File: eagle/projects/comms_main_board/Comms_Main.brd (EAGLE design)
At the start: 160 x 100 mm, 187 parts, among them J1 WRL-00593, J10 MOL-SL-2-RA, J11 MOL-SL-3-RA, J12 MOL-SL-3-RA, J13 MOL-SL-3-RA, J14 MOL-SL-3-RA, J15 MOL-SL-2-RA, J16 MOL-MINIJR-2P-RA, J17 MOL-MINIJR-2P-RA, J18 MOL-MINIJR-2P-RA, J19 MOL-MINIJR-2P-RA, J2 PRT-12639, J20 MOL-SL-2-RA, J21 RECEPTACLE-2x2-254MM, J22 MOL-SL-2-RA, J3 PRT-12639, J4 PRT-12639, J5 PRT-12639, J6 MOL-SL-3-RA, J7 MOL-SL-5-RA, J8 RECEPTACLE-2x20-254MM, J9 MOL-SL-3-RA, Q1 CSD17579Q3A, U1 TPS562209DDCT, U10 MCP4541-103E/MS, U11 TPS562209DDCT, U12 MMBT3904-7-F, U13 MAX3232CSE+, U14 MAX4311, U15 MAX6371, U2 LP2985-33DBVR, U3 LP5900TLX-3.3/NOPB, U4 TPS562209DDCT, U6 LM3488MMX/NOPB, U7 PCT2075D,118, U8 MS560702BA03-50, U9 MAX-M8Q

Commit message: Made ferrite bead part and added to schematic on GPS module I2C line
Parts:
- added FB1, FB2: BLM15HD102SN1D, comms:FB0402
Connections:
- new net GPS_SCL: FB2.2, U9.17_SCL2
- new net GPS_SDA: FB1.2, U9.16_SDA2
- net SCL: now also FB2.1; no longer U9.17_SCL2
- net SDA: now also FB1.1; no longer U9.16_SDA2
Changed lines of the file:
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@@
 <attribute name="VENDOR" value="Digi-Key" x="-477.52" y="-262.89" size="1.778" layer="27" display="off"/>
 </element>
+<element name="FB1" library="comms" package="FB0402" value="BLM15HD102SN1D" x="-486.41" y="-270.51">
+<attribute name="VENDOR_PN" value="490-4003-1-ND" x="-486.41" y="-270.51" size="1.778" layer="27" display="off"/>
+<attribute name="MANUFACTURER" value="Murata" x="-486.41" y="-270.51" size="1.778" layer="27" display="off"/>
+<attribute name="IMPEDANCE" value="1kOhm @100MHz" x="-486.41" y="-270.51" size="1.778" layer="27" display="off"/>
+<attribute name="MANUFACTURER_PN" value="BLM15HD102SN1D" x="-486.41" y="-270.51" size="1.778" layer="27" display="off"/>
+<attribute name="DCR_MAX" value="1.25 Ohm" x="-486.41" y="-270.51" size="1.778" layer="27" display="off"/>
+<attribute name="MAX_CURRENT" value="250mA" x="-486.41" y="-270.51" size="1.778" layer="27" display="off"/>
+<attribute name="VENDOR" value="Digi-Key" x="-486.41" y="-270.51" size="1.778" layer="27" display="off"/>
+</element>
+<element name="FB2" library="comms" package="FB0402" value="BLM15HD102SN1D" x="-486.41" y="-275.59">
+<attribute name="VENDOR_PN" value="490-4003-1-ND" x="-486.41" y="-275.59" size="1.778" layer="27" display="off"/>
+<attribute name="MANUFACTURER" value="Murata" x="-486.41" y="-275.59" size="1.778" layer="27" display="off"/>
+<attribute name="IMPEDANCE" value="1kOhm @100MHz" x="-486.41" y="-275.59" size="1.778" layer="27" display="off"/>
+<attribute name="MANUFACTURER_PN" value="BLM15HD102SN1D" x="-486.41" y="-275.59" size="1.778" layer="27" display="off"/>
+<attribute name="DCR_MAX" value="1.25 Ohm" x="-486.41" y="-275.59" size="1.778" layer="27" display="off"/>
+<attribute name="MAX_CURRENT" value="250mA" x="-486.41" y="-275.59" size="1.778" layer="27" display="off"/>
+<attribute name="VENDOR" value="Digi-Key" x="-486.41" y="-275.59" size="1.778" layer="27" display="off"/>
+</element>
 </elements>
 <signals>
@@
 </signal>
 <signal name="SCL">
-<contactref element="U9" pad="17_SCL2"/>
 <contactref element="R49" pad="2"/>
 <contactref element="R51" pad="2"/>
@@
 <wire x1="127.1016" y1="28.8036" x2="109.4994" y2="28.8036" width="0.254" layer="16"/>
 <wire x1="137.16" y1="38.862" x2="127.1016" y2="28.8036" width="0.254" layer="16"/>
-<wire x1="104.6988" y1="44.8056" x2="104.67" y2="44.91" width="0.254" layer="1"/>
 <wire x1="143.3322" y1="81.3816" x2="142.4178" y2="81.3816" width="0.254" layer="16"/>
 <wire x1="144.4752" y1="82.5246" x2="143.3322" y2="81.3816" width="0.254" layer="16"/>
@@
 <contactref element="R26" pad="1"/>
 <contactref element="TP44" pad="TP"/>
-<wire x1="-440.69" y1="-168.91" x2="-346.29" y2="-130.81" width="0" layer="19" extent="1-1"/>
+<contactref element="FB2" pad="1"/>
+<wire x1="-440.69" y1="-168.91" x2="-486.785" y2="-275.59" width="0" layer="19" extent="1-1"/>
+<wire x1="-346.29" y1="-130.81" x2="-440.69" y2="-168.91" width="0" layer="19" extent="1-1"/>
 <wire x1="-20.32" y1="-6.35" x2="-346.29" y2="-130.81" width="0" layer="19" extent="1-1"/>
 <wire x1="10.287" y1="19.2024" x2="-20.32" y2="-6.35" width="0" layer="19" extent="1-1"/>
@@
 </signal>
 <signal name="SDA">
-<contactref element="U9" pad="16_SDA2"/>
 <contactref element="R48" pad="2"/>
 <contactref element="R50" pad="2"/>
@@
 <wire x1="137.8458" y1="41.3766" x2="136.7028" y2="41.3766" width="0.254" layer="16"/>
 <wire x1="139.6746" y1="39.5478" x2="137.8458" y2="41.3766" width="0.254" layer="16"/>
-<wire x1="104.4702" y1="45.9486" x2="104.67" y2="46.01" width="0.254" layer="1"/>
 <wire x1="142.1892" y1="75.6666" x2="142.1892" y2="78.6384" width="0.254" layer="16"/>
 <wire x1="142.1892" y1="72.9234" x2="142.1892" y2="75.6666" width="0.254" layer="1"/>
@@
 <contactref element="R25" pad="1"/>
 <contactref element="TP43" pad="TP"/>
-<wire x1="-440.69" y1="-165.1" x2="-346.29" y2="-127" width="0" layer="19" extent="1-1"/>
+<contactref element="FB1" pad="1"/>
+<wire x1="-440.69" y1="-165.1" x2="-486.785" y2="-270.51" width="0" layer="19" extent="1-1"/>
+<wire x1="-346.29" y1="-127" x2="-440.69" y2="-165.1" width="0" layer="19" extent="1-1"/>
 <wire x1="-22.86" y1="-6.35" x2="-346.29" y2="-127" width="0" layer="19" extent="1-1"/>
 <wire x1="11.43" y1="14.24" x2="-22.86" y2="-6.35" width="0" layer="19" extent="1-1"/>
@@
 <wire x1="11.43" y1="81.01" x2="93.345" y2="77.21" width="0" layer="19" extent="1-1"/>
 </signal>
+<signal name="GPS_SDA">
+<contactref element="U9" pad="16_SDA2"/>
+<contactref element="FB1" pad="2"/>
+<wire x1="104.67" y1="46.01" x2="-486.035" y2="-270.51" width="0" layer="19" extent="1-1"/>
+</signal>
+<signal name="GPS_SCL">
+<contactref element="FB2" pad="2"/>
+<contactref element="U9" pad="17_SCL2"/>
+<wire x1="104.67" y1="44.91" x2="-486.035" y2="-275.59" width="0" layer="19" extent="1-1"/>
+</signal>
 </signals>

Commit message: Separated the Boost grounds
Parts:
- added SH1: SHORT-HT5, comms:SHORT_TOP-50
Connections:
- new net AGND: SH1.1, U6.4
- net GND: now also SH1.2; no longer U6.4
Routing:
- net GND: track 733.1 -> 732.1 mm
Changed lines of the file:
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@@
 <attribute name="VENDOR" value="Digi-Key" x="-486.41" y="-275.59" size="1.778" layer="27" display="off"/>
 </element>
+<element name="SH1" library="comms" package="SHORT_TOP-50" value="SHORT-HT5" x="-485.14" y="-279.4">
+<attribute name="BOM" value="no" x="-485.14" y="-279.4" size="1.778" layer="27" display="off"/>
+</element>
 </elements>
 <signals>
@@
 <contactref element="C6" pad="2"/>
 <contactref element="C7" pad="2"/>
-<contactref element="R9" pad="1"/>
-<contactref element="U6" pad="4"/>
-<contactref element="U6" pad="5"/>
-<contactref element="C16" pad="2"/>
-<contactref element="C19" pad="2"/>
-<contactref element="R13" pad="1"/>
 <contactref element="U3" pad="3"/>
 <contactref element="C8" pad="2"/>
@@
 <wire x1="11.43" y1="60.1218" x2="12.8016" y2="61.4934" width="0.254" layer="1"/>
 <wire x1="15.0876" y1="61.722" x2="15.24" y2="61.81" width="0.254" layer="1"/>
-<wire x1="12.573" y1="57.3786" x2="11.43" y2="56.2356" width="0.254" layer="1"/>
-<wire x1="12.573" y1="58.7502" x2="12.573" y2="57.3786" width="0.254" layer="1"/>
-<wire x1="11.43" y1="59.8932" x2="12.573" y2="58.7502" width="0.254" layer="1"/>
-<wire x1="11.43" y1="59.8932" x2="11.43" y2="59.96" width="0.254" layer="1"/>
 <wire x1="9.8298" y1="46.863" x2="7.7724" y2="46.863" width="0.254" layer="1"/>
 <wire x1="11.43" y1="48.4632" x2="9.8298" y2="46.863" width="0.254" layer="1"/>
@@
 <wire x1="10.287" y1="53.4924" x2="10.287" y2="55.0926" width="0.254" layer="1"/>
 <wire x1="11.43" y1="52.3494" x2="10.287" y2="53.4924" width="0.254" layer="1"/>
-<wire x1="11.43" y1="52.3494" x2="11.43" y2="52.34" width="0.254" layer="1"/>
 <wire x1="9.6012" y1="69.4944" x2="8.6868" y2="69.4944" width="0.254" layer="1"/>
 <wire x1="8.6868" y1="69.4944" x2="7.7724" y2="69.4944" width="0.254" layer="1"/>
@@
 <wire x1="12.573" y1="81.6102" x2="12.573" y2="80.2386" width="0.254" layer="1"/>
 <wire x1="11.43" y1="82.7532" x2="12.573" y2="81.6102" width="0.254" layer="1"/>
-<wire x1="15.0876" y1="77.2668" x2="15.24" y2="77.05" width="0.254" layer="1"/>
 <wire x1="11.43" y1="82.7532" x2="11.43" y2="82.82" width="0.254" layer="1"/>
 <wire x1="13.2588" y1="92.3544" x2="15.0876" y2="92.3544" width="0.254" layer="1"/>
@@
 <wire x1="11.8872" y1="86.6394" x2="13.716" y2="88.4682" width="0.254" layer="1"/>
 <wire x1="11.43" y1="86.6394" x2="11.8872" y2="86.6394" width="0.254" layer="1"/>
-<wire x1="15.0876" y1="88.4682" x2="15.24" y2="88.48" width="0.254" layer="1"/>
 <wire x1="9.8298" y1="85.0392" x2="9.3726" y2="85.0392" width="0.254" layer="1"/>
 <wire x1="9.3726" y1="85.0392" x2="7.7724" y2="85.0392" width="0.254" layer="1"/>
@@
 <wire x1="12.573" y1="66.5226" x2="12.573" y2="63.0936" width="0.254" layer="1"/>
 <wire x1="11.43" y1="67.6656" x2="12.573" y2="66.5226" width="0.254" layer="1"/>
-<wire x1="11.43" y1="60.1218" x2="11.43" y2="59.96" width="0.254" layer="1"/>
 <wire x1="11.43" y1="67.6656" x2="11.43" y2="67.58" width="0.254" layer="1"/>
 <wire x1="6.6294" y1="35.2044" x2="7.3152" y2="35.2044" width="0.254" layer="1"/>
@@
 <wire x1="84.582" y1="62.4078" x2="84.1248" y2="62.4078" width="0.254" layer="1"/>
 <wire x1="76.3524" y1="79.5528" x2="76.37" y2="79.385" width="0.254" layer="1"/>
-<wire x1="84.582" y1="62.4078" x2="84.7471" y2="62.525" width="0.254" layer="1"/>
 <wire x1="82.296" y1="62.4078" x2="80.4672" y2="62.4078" width="0.254" layer="1"/>
 <wire x1="83.2104" y1="63.3222" x2="82.296" y2="62.4078" width="0.254" layer="1"/>
-<wire x1="80.4672" y1="62.4078" x2="80.3529" y2="62.525" width="0.254" layer="1"/>
 <wire x1="76.581" y1="86.1822" x2="77.9526" y2="86.1822" width="0.254" layer="1"/>
 <wire x1="77.0382" y1="86.1822" x2="76.581" y2="86.1822" width="0.254" layer="16"/>
@@
 <contactref element="C37" pad="2"/>
 <contactref element="C14" pad="2"/>
+<contactref element="C12" pad="2"/>
+<contactref element="C16" pad="2"/>
 <contactref element="C15" pad="2"/>
 <contactref element="C17" pad="2"/>
 <contactref element="C18" pad="2"/>
+<contactref element="R9" pad="1"/>
+<contactref element="U6" pad="5"/>
+<contactref element="C19" pad="2"/>
+<contactref element="R13" pad="1"/>
 <contactref element="R6" pad="1"/>
 <contactref element="L4" pad="2"/>
 <contactref element="C21" pad="2"/>
-<contactref element="C12" pad="2"/>
+<wire x1="12.573" y1="57.3786" x2="11.43" y2="56.2356" width="0.254" layer="1"/>
+<wire x1="12.573" y1="58.7502" x2="12.573" y2="57.3786" width="0.254" layer="1"/>
+<wire x1="11.43" y1="59.8932" x2="12.573" y2="58.7502" width="0.254" layer="1"/>
+<wire x1="11.43" y1="59.8932" x2="11.43" y2="59.96" width="0.254" layer="1"/>
+<contactref element="SH1" pad="2"/>
 <wire x1="-260.35" y1="-17.3482" x2="-234.95" y2="-17.3482" width="0" layer="19" extent="1-1"/>
 <wire x1="-285.75" y1="-17.3482" x2="-260.35" y2="-17.3482" width="0" layer="19" extent="1-1"/>
@@
 <wire x1="15.3162" y1="37.2618" x2="15.24" y2="37.25" width="0" layer="19" extent="1-1"/>
 <wire x1="11.43" y1="48.6918" x2="11.43" y2="48.4632" width="0" layer="19" extent="1-1"/>
+<wire x1="11.43" y1="52.34" x2="11.43" y2="52.3494" width="0" layer="19" extent="1-1"/>
 <wire x1="11.43" y1="56.2356" x2="11.43" y2="56.007" width="0" layer="19" extent="1-1"/>
+<wire x1="11.43" y1="60.1218" x2="11.43" y2="59.96" width="0" layer="19" extent="1-1"/>
+<wire x1="15.24" y1="88.48" x2="15.0876" y2="88.4682" width="0" layer="19" extent="1-1"/>
+<wire x1="15.24" y1="77.05" x2="15.0876" y2="77.2668" width="0" layer="19" extent="1-1"/>
 <wire x1="100.3554" y1="39.5478" x2="86.868" y2="28.575" width="0" layer="19" extent="1-16"/>
 <wire x1="100.3554" y1="39.5478" x2="100.3554" y2="39.5478" width="0" layer="19" extent="1-16"/>
-<wire x1="91.44" y1="66.294" x2="94.6404" y2="52.8066" width="0" layer="19" extent="1-1"/>
+<wire x1="84.7471" y1="62.525" x2="94.6404" y2="52.8066" width="0" layer="19" extent="1-1"/>
+<wire x1="84.582" y1="62.4078" x2="84.7471" y2="62.525" width="0" layer="19" extent="1-1"/>
 <wire x1="98.5266" y1="84.8106" x2="97.155" y2="82.81" width="0" layer="19" extent="1-1"/>
 <wire x1="97.05" y1="86.36" x2="97.155" y2="86.1822" width="0" layer="19" extent="1-1"/>
@@
 <wire x1="-468.52" y1="-246.38" x2="-452.39" y2="-247.65" width="0" layer="19" extent="1-1"/>
 <wire x1="-474.4" y1="-262.89" x2="-468.52" y2="-246.38" width="0" layer="19" extent="1-1"/>
+<wire x1="-485.775" y1="-279.4" x2="-474.4" y2="-262.89" width="0" layer="19" extent="1-1"/>
 </signal>
 <signal name="7P4V_IN">
@@
 <wire x1="104.67" y1="44.91" x2="-486.035" y2="-275.59" width="0" layer="19" extent="1-1"/>
 </signal>
+<signal name="AGND">
+<contactref element="U6" pad="4"/>
+<contactref element="SH1" pad="1"/>
+<wire x1="-484.505" y1="-279.4" x2="80.3529" y2="62.525" width="0" layer="19" extent="1-1"/>
+</signal>
 </signals>

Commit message: Begin component placement
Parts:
- moved L4 653.8 mm to (111.8, 39.4)
- moved FB1 593.7 mm to (-27.9, 106.7)
- moved FB2 583.4 mm to (-45.7, 106.7)
- moved C21 563.7 mm to (-33.0, 83.8)
- moved SH1 545.4 mm to (-113.0, 119.4)
- moved C17 542.5 mm to (-57.1, 127.0)
- moved OUTLINE1 539.2 mm to (1.91, 63.5)
- moved TP49 522.0 mm to (-17.8, 118.1)
- moved TP50 519.2 mm to (-24.1, 118.1)
- moved TP51 516.4 mm to (-30.5, 118.1)
- moved R6 513.8 mm to (-80.0, 100.3)
- moved TP52 513.7 mm to (-36.8, 118.1)
- moved TP53 511.1 mm to (-43.2, 118.1)
- moved R5 510.3 mm to (-99.1, 127.0)
- moved TP54 508.6 mm to (-49.5, 118.1)
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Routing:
- net GND: track 732.1 -> 0.00 mm, vias 19 -> 0
- net 5V_BOARD: track 501.4 -> 0.00 mm, vias 22 -> 0
- net 3P3V_SENSORS: track 336.6 -> 0.00 mm, vias 14 -> 0
- net SDA: track 330.4 -> 0.00 mm, vias 17 -> 0
- net PI_BUCK_SW: track 330.3 -> 0.00 mm, vias 7 -> 0
- net 11P1V_IN: track 321.5 -> 0.00 mm, vias 17 -> 0
- net GPS_ANTENNA: track 296.5 -> 0.00 mm, vias 11 -> 0
- net 12V_BOARD: track 288.1 -> 0.00 mm, vias 12 -> 0
- net 3P3V_DIG_POT: track 278.3 -> 0.00 mm, vias 15 -> 0
- net 7P4V_IN: track 271.7 -> 0.00 mm, vias 15 -> 0
- net RX_OUT_S: track 264.2 -> 0.00 mm, vias 4 -> 0
- net SCL: track 257.7 -> 0.00 mm, vias 6 -> 0
- net POT_SDA: track 255.4 -> 0.00 mm, vias 8 -> 0
- net RX_IN_T: track 250.4 -> 0.00 mm, vias 4 -> 0
- net PI_BUCK_VBST: track 244.2 -> 0.00 mm, vias 8 -> 0
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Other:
- board size 160 x 100 mm -> 101.6 x 95.2 mm

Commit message: Component placement sonnn
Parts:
- moved R15 244.4 mm to (95.6, 15.7), flipped to the bottom
- moved R14 242.0 mm to (95.6, 13.5), flipped to the bottom
- moved L3 238.6 mm to (126.3, 44.7)
- moved C19 211.7 mm to (79.7, 35.7)
- moved C20 209.0 mm to (66.6, 23.0)
- moved R53 206.9 mm to (91.9, 15.6), flipped to the bottom
- moved R52 205.0 mm to (91.7, 13.2), flipped to the bottom
- moved R11 204.5 mm to (77.8, 38.6)
- moved C18 204.1 mm to (79.2, 44.9)
- moved C29 198.9 mm to (93.9, 17.9), flipped to the bottom
- moved SH1 197.9 mm to (59.3, 22.0)
- moved D1 196.0 mm to (67.3, 59.7)
- moved R13 191.4 mm to (60.3, 48.5)
- moved R5 191.0 mm to (61.4, 23.5)
- moved R12 187.9 mm to (55.7, 39.4)
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
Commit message: Update NPN BJT digikey numbers
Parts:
- U12: value MMBT3904-7-F -> MMBT3904-HF
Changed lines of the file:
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@@
 <attribute name="VENDOR" value="Digi-Key" x="75.2365125" y="35.48586875" size="1.778" layer="27" display="off"/>
 </element>
-<element name="U12" library="comms" package="SOT103P240X110-3N" value="MMBT3904-7-F" x="81.504734375" y="71.1496125">
-<attribute name="VENDOR_PN" value="MMBT3904-FDICT-ND" x="81.504734375" y="71.1496125" size="1.778" layer="27" display="off"/>
-<attribute name="MANUFACTURER_PN" value="MMBT3904-7-F" x="81.504734375" y="71.1496125" size="1.778" layer="27" display="off"/>
-<attribute name="MANUFACTURER" value="Diodes, Inc" x="81.504734375" y="71.1496125" size="1.778" layer="27" display="off"/>
+<element name="U12" library="comms" package="SOT103P240X110-3N" value="MMBT3904-HF" x="81.504734375" y="71.1496125">
+<attribute name="VENDOR_PN" value="641-1683-1-ND" x="81.504734375" y="71.1496125" size="1.778" layer="27" display="off"/>
+<attribute name="MANUFACTURER_PN" value="MMBT3904-HF" x="81.504734375" y="71.1496125" size="1.778" layer="27" display="off"/>
+<attribute name="MANUFACTURER" value="Comchip" x="81.504734375" y="71.1496125" size="1.778" layer="27" display="off"/>
 <attribute name="VENDOR" value="Digikey" x="81.504734375" y="71.1496125" size="1.778" layer="27" display="off"/>
 </element>

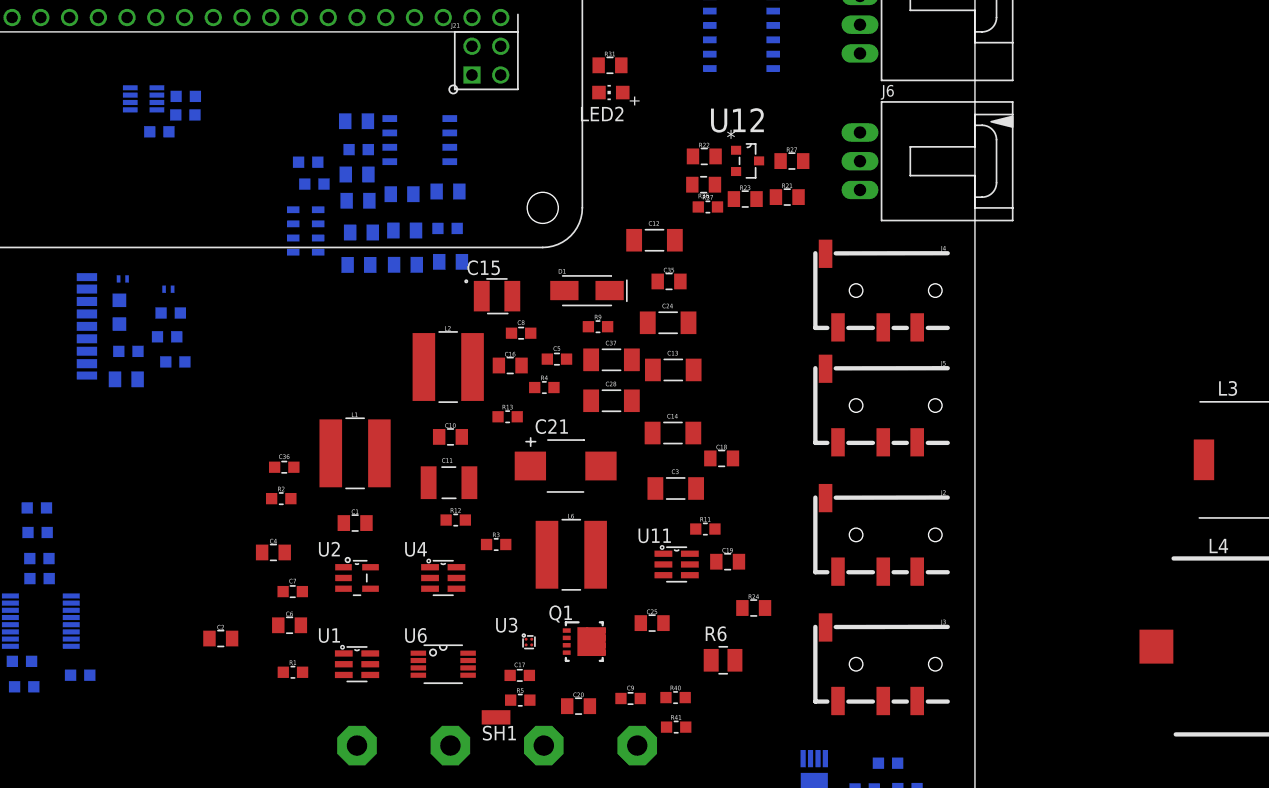
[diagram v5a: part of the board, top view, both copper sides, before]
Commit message: Component placement refinements
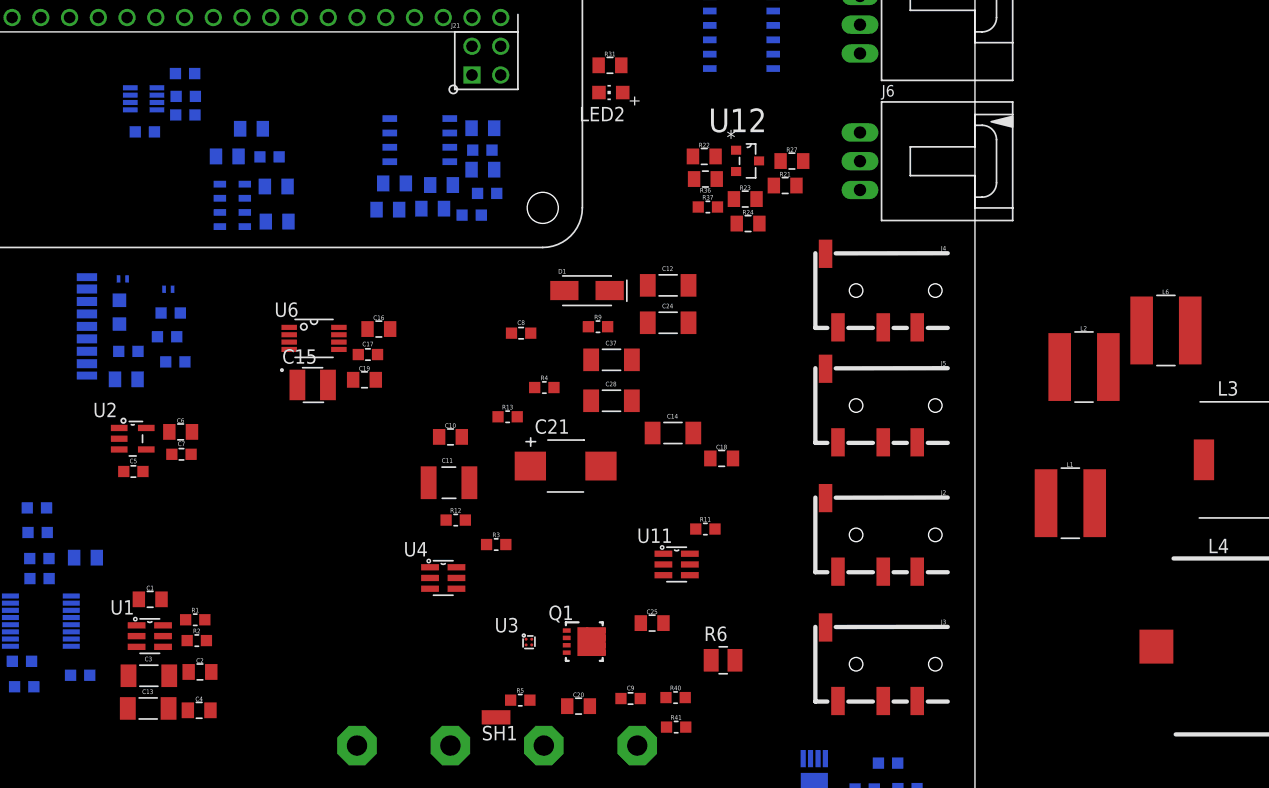
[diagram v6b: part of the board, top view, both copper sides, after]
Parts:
- moved L1 63.4 mm to (110.0, 40.9)
- moved C35 57.1 mm to (23.0, 36.1), flipped to the bottom
- moved L2 56.2 mm to (111.2, 52.9)
- moved L6 56.2 mm to (118.5, 56.2)
- moved C13 55.2 mm to (28.5, 22.8)
- moved C3 49.4 mm to (28.6, 25.7)
- moved C5 38.7 mm to (27.2, 43.7)
- moved C19 35.9 mm to (47.6, 51.8)
- moved R24 34.0 mm to (81.5, 65.6)
- moved C36 32.1 mm to (28.2, 73.7), flipped to the bottom
- moved C17 31.4 mm to (48.0, 54.0)
- moved U6 31.0 mm to (43.2, 55.5)
- moved U2 23.3 mm to (27.2, 46.6)
- moved C6 19.6 mm to (31.4, 47.2)
- moved C1 19.3 mm to (28.7, 32.4)
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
